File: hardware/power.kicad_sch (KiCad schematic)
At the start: 32 parts, among them J401 PRPC001DAAN-RC, J402 Conn_01x01, J403 Conn_01x01, J404 PRPC001DAAN-RC, J405 PRPC001DAAN-RC, J406 PRPC001DAAN-RC, U401 LM66200DRLR, U402 TPS63020DSJR

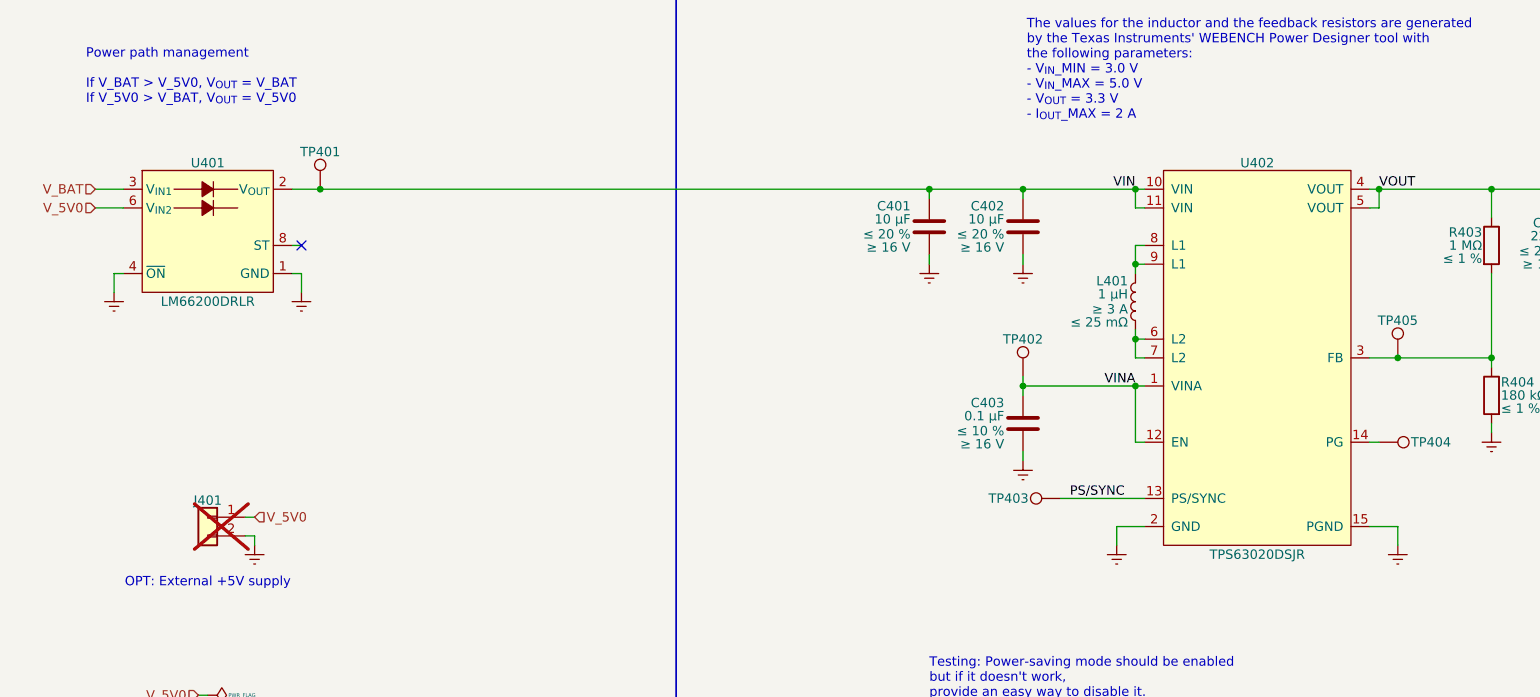
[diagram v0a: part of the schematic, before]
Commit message: HW: Update libraries, fix typos, refine schematics
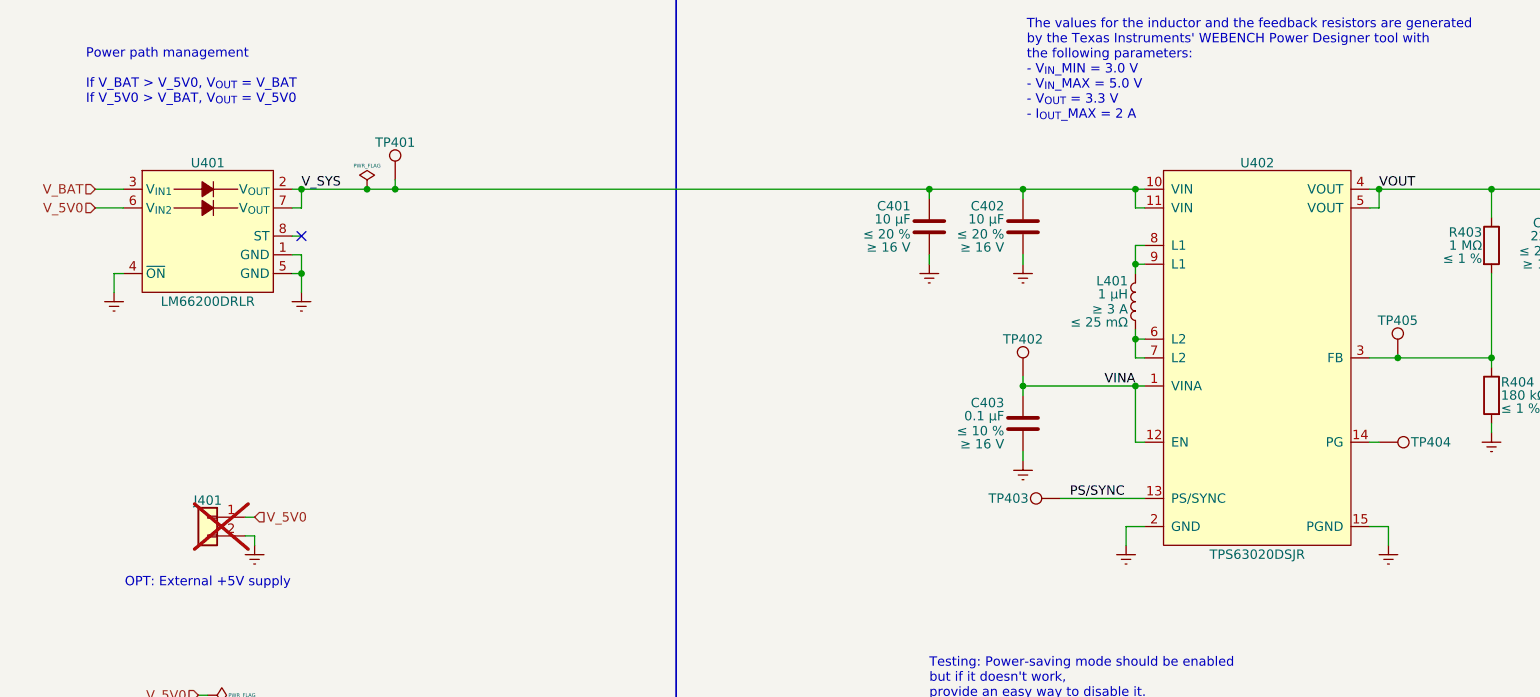
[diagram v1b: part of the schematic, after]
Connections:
- net VIN renamed V_SYS
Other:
- moved on the sheet: TP401
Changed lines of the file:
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@@
 	)
 	(junction
-		(at 82.55 152.4)
-		(diameter 0)
-		(color 0 0 0 0)
-	)
-	(junction
 		(at 241.3 152.4)
 		(diameter 0)
@@
 	)
 	(junction
+		(at 80.01 163.83)
+		(diameter 0)
+		(color 0 0 0 0)
+	)
+	(junction
 		(at 193.04 152.4)
 		(diameter 0)
@@
 	)
 	(junction
+		(at 92.71 152.4)
+		(diameter 0)
+		(color 0 0 0 0)
+	)
+	(junction
 		(at 180.34 228.6)
 		(diameter 0)
@@
 	)
 	(junction
+		(at 88.9 152.4)
+		(diameter 0)
+		(color 0 0 0 0)
+	)
+	(junction
 		(at 334.01 152.4)
 		(diameter 0)
@@
 	)
 	(junction
+		(at 80.01 152.4)
+		(diameter 0)
+		(color 0 0 0 0)
+	)
+	(junction
 		(at 177.8 152.4)
 		(diameter 0)
@@
 	)
 	(no_connect
-		(at 80.01 160.02)
+		(at 80.01 158.75)
 	)
 	(wire
@@
 	(wire
 		(pts
+			(xy 88.9 152.4) (xy 92.71 152.4)
+		)
+		(stroke
+			(width 0)
+			(type default)
+		)
+	)
+	(wire
+		(pts
+			(xy 80.01 161.29) (xy 80.01 163.83)
+		)
+		(stroke
+			(width 0)
+			(type default)
+		)
+	)
+	(wire
+		(pts
 			(xy 226.06 186.69) (xy 224.79 186.69)
 		)
@@
 	(wire
 		(pts
-			(xy 228.6 200.66) (xy 228.6 198.12)
+			(xy 227.33 200.66) (xy 227.33 198.12)
 		)
 		(stroke
@@
 	(wire
 		(pts
-			(xy 190.5 198.12) (xy 194.31 198.12)
+			(xy 191.77 198.12) (xy 194.31 198.12)
 		)
 		(stroke
@@
 	(wire
 		(pts
+			(xy 78.74 161.29) (xy 80.01 161.29)
+		)
+		(stroke
+			(width 0)
+			(type default)
+		)
+	)
+	(wire
+		(pts
 			(xy 241.3 152.4) (xy 254 152.4)
 		)
@@
 	(wire
 		(pts
+			(xy 92.71 152.4) (xy 165.1 152.4)
+		)
+		(stroke
+			(width 0)
+			(type default)
+		)
+	)
+	(wire
+		(pts
 			(xy 241.3 156.21) (xy 241.3 152.4)
 		)
@@
 	(wire
 		(pts
-			(xy 228.6 198.12) (xy 224.79 198.12)
+			(xy 227.33 198.12) (xy 224.79 198.12)
 		)
 		(stroke
@@
 	(wire
 		(pts
+			(xy 80.01 154.94) (xy 80.01 152.4)
+		)
+		(stroke
+			(width 0)
+			(type default)
+		)
+	)
+	(wire
+		(pts
 			(xy 241.3 163.83) (xy 241.3 175.26)
 		)
@@
 	(wire
 		(pts
-			(xy 82.55 152.4) (xy 165.1 152.4)
+			(xy 191.77 200.66) (xy 191.77 198.12)
 		)
 		(stroke
@@
 	(wire
 		(pts
-			(xy 190.5 200.66) (xy 190.5 198.12)
+			(xy 266.7 156.21) (xy 266.7 152.4)
 		)
 		(stroke
@@
 	(wire
 		(pts
-			(xy 266.7 156.21) (xy 266.7 152.4)
+			(xy 194.31 172.72) (xy 193.04 172.72)
 		)
 		(stroke
@@
 	(wire
 		(pts
-			(xy 194.31 172.72) (xy 193.04 172.72)
+			(xy 334.01 179.07) (xy 335.28 179.07)
 		)
 		(stroke
@@
 	(wire
 		(pts
-			(xy 334.01 179.07) (xy 335.28 179.07)
+			(xy 78.74 154.94) (xy 80.01 154.94)
 		)
 		(stroke
@@
 	(wire
 		(pts
-			(xy 78.74 152.4) (xy 82.55 152.4)
+			(xy 78.74 152.4) (xy 80.01 152.4)
 		)
 		(stroke
@@
 	(wire
 		(pts
-			(xy 80.01 160.02) (xy 78.74 160.02)
+			(xy 92.71 151.13) (xy 92.71 152.4)
+		)
+		(stroke
+			(width 0)
+			(type default)
+		)
+	)
+	(wire
+		(pts
+			(xy 80.01 158.75) (xy 78.74 158.75)
+		)
+		(stroke
+			(width 0)
+			(type default)
+		)
+	)
+	(wire
+		(pts
+			(xy 80.01 152.4) (xy 88.9 152.4)
 		)
 		(stroke
@@
 		)
 	)
-	(label "VIN"
-		(at 193.04 152.4 180)
+	(label "V_SYS"
+		(at 80.01 152.4 0)
 		(effects
 			(font
 				(size 1.27 1.27)
 			)
-			(justify right bottom)
+			(justify left bottom)
 		)
 	)
@@
 	(symbol
 		(lib_id "power:Earth")
-		(at 228.6 200.66 0)
+		(at 227.33 200.66 0)
 		(mirror y)
 		(unit 1)
@@
 		(fields_autoplaced yes)
 		(property "Reference" "#PWR0410"
-			(at 228.6 207.01 0)
+			(at 227.33 207.01 0)
 			(effects
 				(font
@@
 		)
 		(property "Value" "GND"
-			(at 228.6 205.74 0)
+			(at 227.33 205.74 0)
 			(effects
 				(font
@@
 		)
 		(property "Footprint" ""
-			(at 228.6 200.66 0)
+			(at 227.33 200.66 0)
 			(effects
 				(font
@@
 		)
 		(property "Datasheet" "~"
-			(at 228.6 200.66 0)
+			(at 227.33 200.66 0)
 			(effects
 				(font
@@
 		)
 		(property "Description" "Power symbol creates a global label with name \"Earth\""
-			(at 228.6 200.66 0)
+			(at 227.33 200.66 0)
 			(effects
 				(font
@@
 	(symbol
 		(lib_id "Connector:TestPoint")
-		(at 82.55 152.4 0)
+		(at 92.71 151.13 0)
 		(unit 1)
 		(exclude_from_sim no)
@@
 		(dnp no)
 		(property "Reference" "TP401"
-			(at 82.55 148.082 0)
+			(at 92.71 146.812 0)
 			(effects
 				(font
@@
 		)
 		(property "Value" "TestPoint"
-			(at 85.09 150.3679 0)
+			(at 95.25 149.0979 0)
 			(effects
 				(font
@@
 		)
 		(property "Footprint" "TestPoint:TestPoint_Pad_D1.0mm"
-			(at 87.63 152.4 0)
+			(at 97.79 151.13 0)
 			(effects
 				(font
@@
 		)
 		(property "Datasheet" "~"
-			(at 87.63 152.4 0)
+			(at 97.79 151.13 0)
 			(effects
 				(font
@@
 		)
 		(property "Description" "test point"
-			(at 82.55 152.4 0)
+			(at 92.71 151.13 0)
 			(effects
 				(font
@@
 	(symbol
 		(lib_id "power:Earth")
-		(at 190.5 200.66 0)
+		(at 191.77 200.66 0)
 		(mirror y)
 		(unit 1)
@@
 		(fields_autoplaced yes)
 		(property "Reference" "#PWR0409"
-			(at 190.5 207.01 0)
+			(at 191.77 207.01 0)
 			(effects
 				(font
@@
 		)
 		(property "Value" "GND"
-			(at 190.5 205.74 0)
+			(at 191.77 205.74 0)
 			(effects
 				(font
@@
 		)
 		(property "Footprint" ""
-			(at 190.5 200.66 0)
+			(at 191.77 200.66 0)
 			(effects
 				(font
@@
 		)
 		(property "Datasheet" "~"
-			(at 190.5 200.66 0)
+			(at 191.77 200.66 0)
 			(effects
 				(font
@@
 		)
 		(property "Description" "Power symbol creates a global label with name \"Earth\""
-			(at 190.5 200.66 0)
+			(at 191.77 200.66 0)
 			(effects
 				(font
@@
 	)
 	(symbol
+		(lib_id "power:PWR_FLAG")
+		(at 88.9 152.4 0)
+		(mirror y)
+		(unit 1)
+		(exclude_from_sim no)
+		(in_bom yes)
+		(on_board yes)
+		(dnp no)
+		(property "Reference" "#FLG0403"
+			(at 88.9 150.495 0)
+			(effects
+				(font
+					(size 1.27 1.27)
+				)
+				(hide yes)
+			)
+		)
+		(property "Value" "PWR_FLAG"
+			(at 88.9 149.225 0)
+			(effects
+				(font
+					(size 0.5 0.5)
+				)
+			)
+		)
+		(property "Footprint" ""
+			(at 88.9 152.4 0)
+			(effects
+				(font
+					(size 1.27 1.27)
+				)
+				(hide yes)
+			)
+		)
+		(property "Datasheet" "~"
+			(at 88.9 152.4 0)
+			(effects
+				(font
+					(size 1.27 1.27)
+				)
+				(hide yes)
+			)
+		)
+		(property "Description" "Special symbol for telling ERC where power comes from"
+			(at 88.9 152.4 0)
+			(effects
+				(font
+					(size 1.27 1.27)
+				)
+				(hide yes)
+			)
+		)
+		(pin "1"
+		)
+		(instances
+			(project "iida_devkit"
+				(path "/b12a6e25-97fb-4aba-bc96-af8db389bb9a/5e1bb3da-9ec5-412a-a6e9-5701708c7ef6"
+					(reference "#FLG0403")
+					(unit 1)
+				)
+			)
+		)
+	)
+	(symbol
 		(lib_id "power:Earth")
 		(at 180.34 238.76 0)
@@
 		(on_board yes)
 		(dnp no)
-		(property "Reference" "#FLG0403"
+		(property "Reference" "#FLG0404"
 			(at 339.09 150.495 0)
 			(effects
@@
 			(project "iida_devkit"
 				(path "/b12a6e25-97fb-4aba-bc96-af8db389bb9a/5e1bb3da-9ec5-412a-a6e9-5701708c7ef6"
-					(reference "#FLG0403")
+					(reference "#FLG0404")
 					(unit 1)
 				)

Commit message: HW: Refine schematics
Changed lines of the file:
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@@
 	(title_block
 		(title "Iida devkit")
-		(date "2025-05-23")
+		(date "2025-05-24")
 		(rev "v5.0.0")
 	)
@@
 		)
 	)
-	(text_box "To ensure no back-feeding occurs, the device can be powered either through the USB-C connection or by using a battery.\n\nIt is important to OR the power inputs to prevent this issue."
+	(text_box "The device can be powered either through the USB-C connection or by using a battery.\n\nOR the power inputs to prevent back-feeding."
 		(exclude_from_sim no)
 		(at 15.24 63.5 0)

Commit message: HW: Update libraries
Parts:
- TP406: footprint TestPoint:TestPoint_Pad_D1.0mm -> Mechanical:TestPoint_Pad_100.0x100.0mm
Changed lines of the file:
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@@
 			)
 		)
-		(property "Footprint" "TestPoint:TestPoint_Pad_D1.0mm"
+		(property "Footprint" "Mechanical:TestPoint_Pad_100.0x100.0mm"
 			(at 325.12 243.84 0)
 			(effects

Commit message: HW: Fix BOM
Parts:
- C403: DigiKey Part Number 490-7998-1-ND -> 732-7532-1-ND; MPN GCM155R71C104KA55J -> 885012205037; Manufacturer Murata Electronics -> Würth Elektronik
- J402, J403: value Conn_01x01 -> 61300111121; now not fitted
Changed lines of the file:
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@@
 			)
 		)
-		(property "Manufacturer" "Murata Electronics"
+		(property "Manufacturer" "Würth Elektronik"
 			(at 177.8 184.15 0)
 			(effects
@@
 			)
 		)
-		(property "MPN" "GCM155R71C104KA55J"
+		(property "MPN" "885012205037"
 			(at 177.8 184.15 0)
 			(effects
@@
 			)
 		)
-		(property "DigiKey Part Number" "490-7998-1-ND"
+		(property "DigiKey Part Number" "732-7532-1-ND"
 			(at 177.8 184.15 0)
 			(effects
@@
 		(in_bom yes)
 		(on_board yes)
-		(dnp no)
+		(dnp yes)
 		(property "Reference" "J403"
 			(at 320.04 226.822 0)
@@
 			)
 		)
-		(property "Value" "Conn_01x01"
+		(property "Value" "61300111121"
 			(at 320.04 224.79 0)
 			(effects
@@
 		(in_bom yes)
 		(on_board yes)
-		(dnp no)
+		(dnp yes)
 		(property "Reference" "J402"
 			(at 320.04 220.472 0)
@@
 			)
 		)
-		(property "Value" "Conn_01x01"
+		(property "Value" "61300111121"
 			(at 320.04 218.44 0)
 			(effects

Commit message: HW: Fix 1cm x 1cm test point
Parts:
- TP406: footprint Mechanical:TestPoint_Pad_100.0x100.0mm -> Mechanical:TestPoint_Pad_10.0x10.0mm
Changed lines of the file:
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@@
 			)
 		)
-		(property "Footprint" "Mechanical:TestPoint_Pad_100.0x100.0mm"
+		(property "Footprint" "Mechanical:TestPoint_Pad_10.0x10.0mm"
 			(at 325.12 243.84 0)
 			(effects

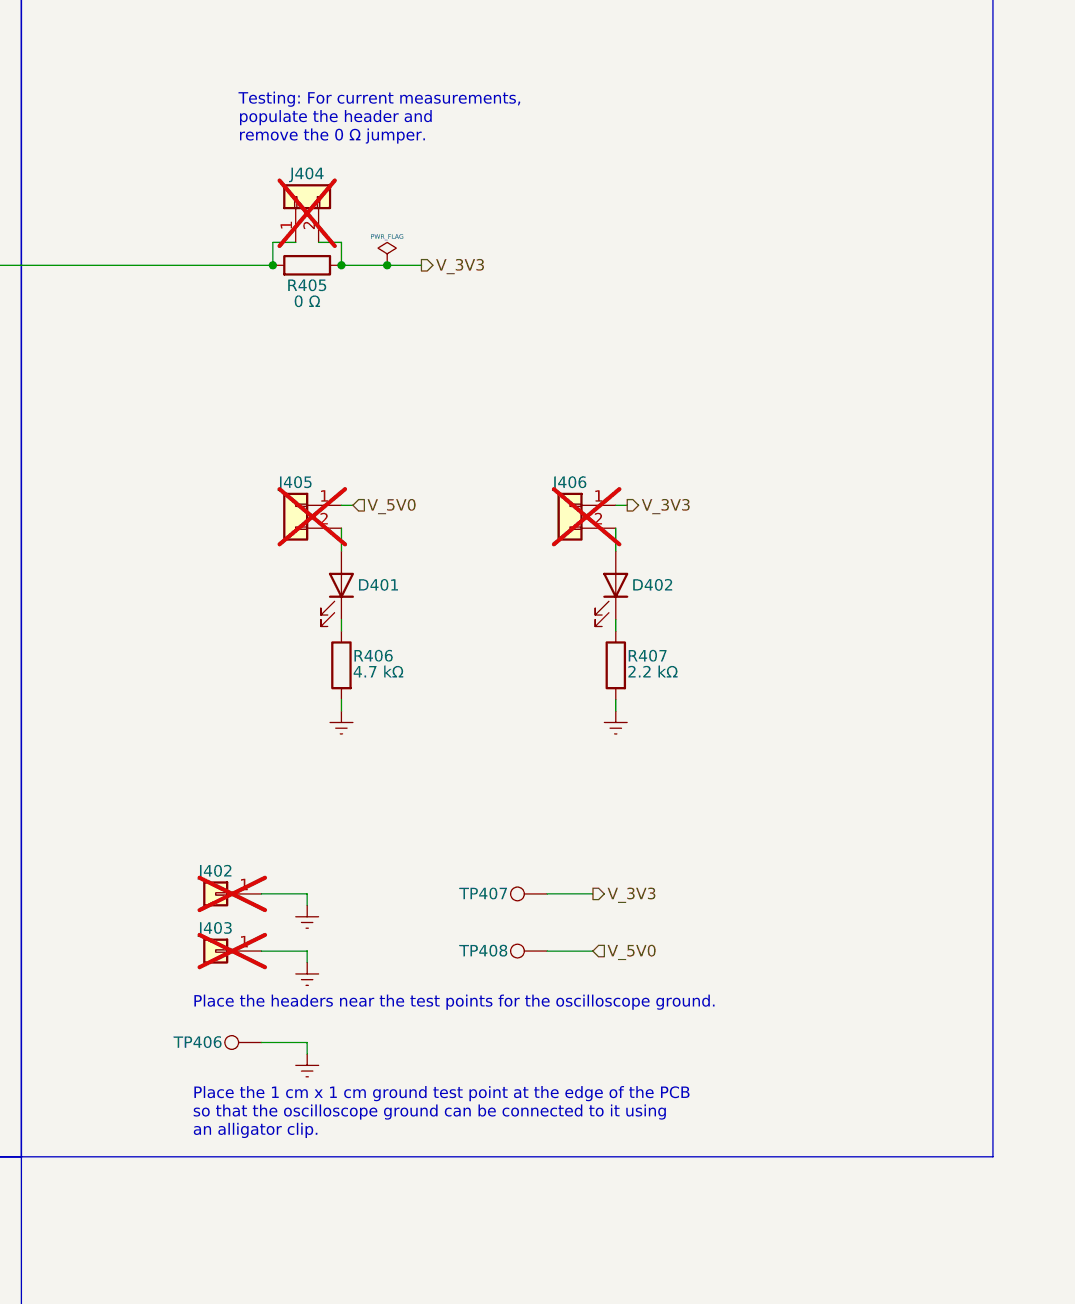
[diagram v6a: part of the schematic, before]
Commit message: HW: Update libraries
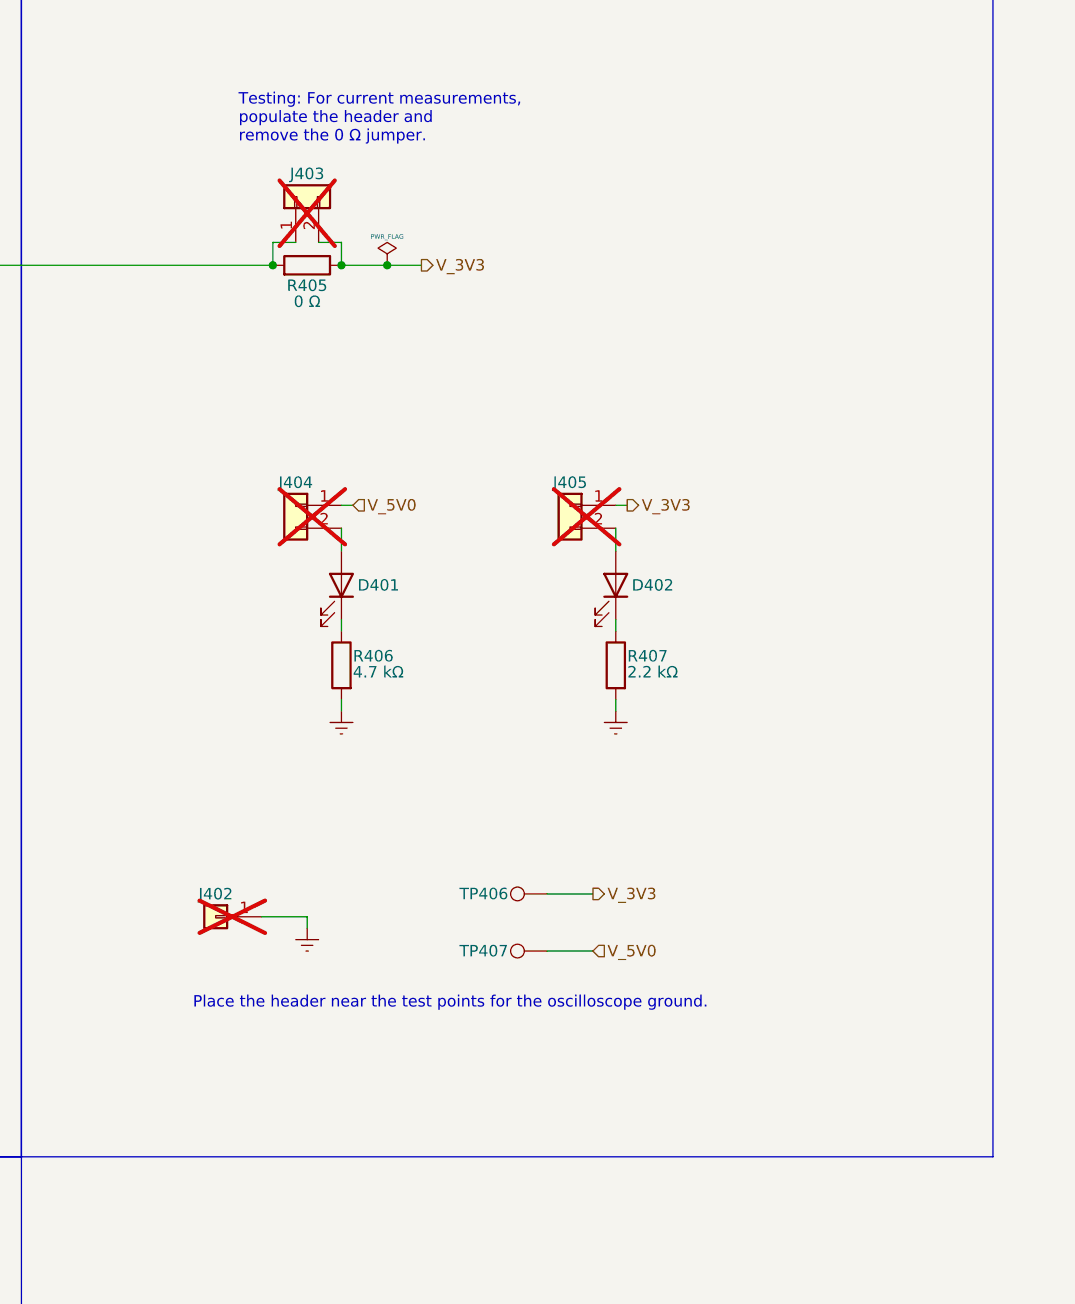
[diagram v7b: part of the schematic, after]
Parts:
- removed J403: 61300111121, Connector_PinHeader_2.54mm:PinHeader_1x01_P2.54mm_Vertical, symbol Connector_Generic:Conn_01x01
- removed TP406: TestPoint, Mechanical:TestPoint_Pad_10.0x10.0mm, symbol Connector:TestPoint
- R401: footprint Resistor_SMD:R_0402_1005Metric -> perfect_footprints:R_0402_1005Metric
- renumbered J404 to J403, J405 to J404, J406 to J405, TP407 to TP406, TP408 to TP407
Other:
- note added: "Place the header near the test points for the oscilloscope ground."
- note removed: "Place the 1 cm x 1 cm ground test point at the edge of the PCB so that the oscilloscope ground can be connected to it using an alligator clip."
- note removed: "Place the headers near the test points for the oscilloscope ground."
- moved on the sheet: J402
